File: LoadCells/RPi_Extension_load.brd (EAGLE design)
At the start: 80 x 50 mm, 42 parts, among them U1 AD7730BRUZ, U2 AD7730BRUZ, U3 AD7730BRUZ, U4 AD7730BRUZ, U5 AD7730BRUZ, U6 AD7730BRUZ, U7 AD7730BRUZ, U8 AD7730BRUZ, U9 STM32F103RCT6, Y1 ABM3B, Y2 KC2520B-C1

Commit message: retouched load cell board
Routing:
- net U1_AIN2_-: track 19.8 -> 24.6 mm
- net U2_AIN2_+: track 22.1 -> 20.5 mm
- net U2_AIN2_-: track 20.0 -> 21.5 mm
- net U2_AIN1_-: track 19.8 -> 18.4 mm
- net U2_AIN1_+: track 23.6 -> 22.4 mm
- net U5_AIN1_+: track 22.9 -> 22.0 mm
- net U1_AIN1_+: track 26.0 -> 25.3 mm
- net U8_AIN2_-: track 7.77 -> 8.43 mm
- net U8_AIN2_+: track 7.44 -> 8.05 mm
- net U6_AIN1_-: track 13.3 -> 13.9 mm

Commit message: added additional id jumpers to adc and dac board
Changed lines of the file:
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@@
 <wire x1="5.82" y1="16.28" x2="5.85" y2="16.28" width="0.4064" layer="16"/>
 <wire x1="5.85" y1="16.28" x2="5.85" y2="13.75" width="1.27" layer="16"/>
-<wire x1="5.82" y1="16.3" x2="5.82" y2="16.28" width="0.4064" layer="1"/>
 <wire x1="5.82" y1="13.65" x2="5.82" y2="13.74" width="0.4064" layer="16"/>
 </signal>

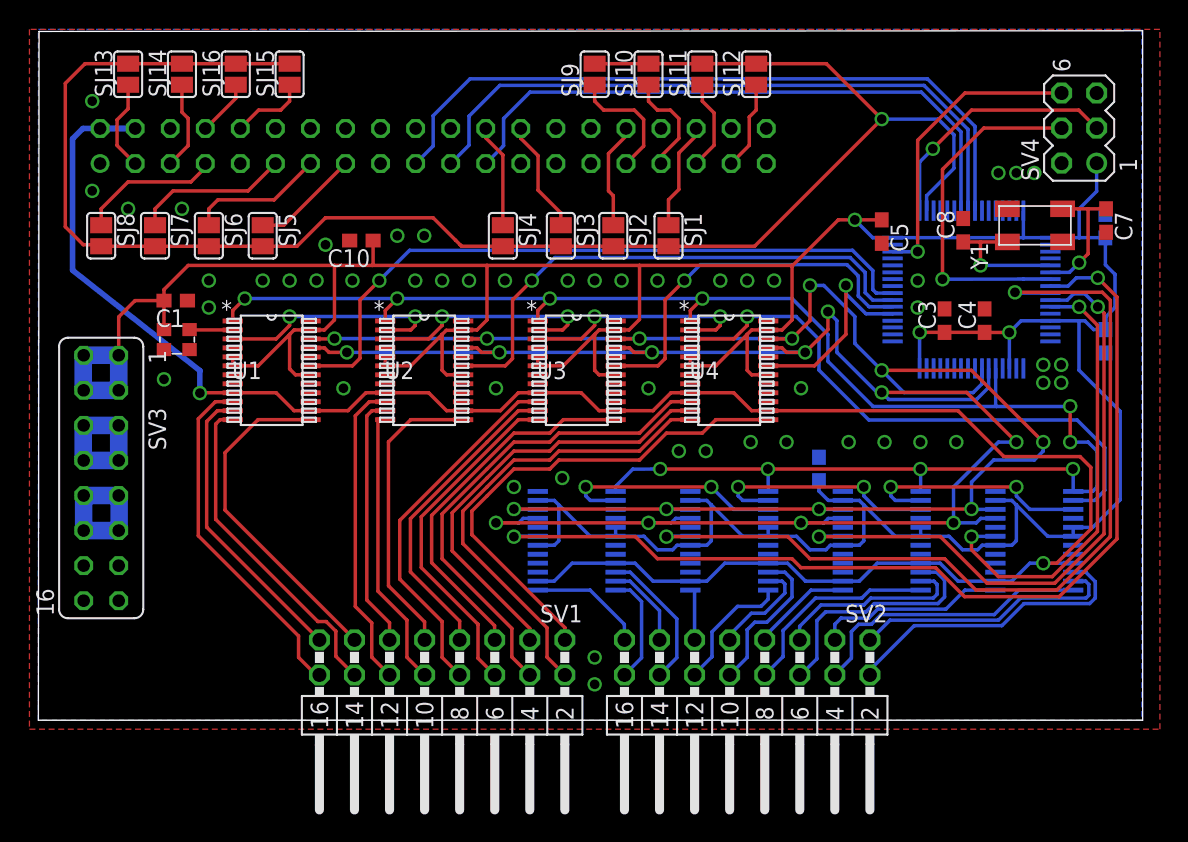
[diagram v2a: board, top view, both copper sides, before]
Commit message: cleaned up silklayer of load cell board
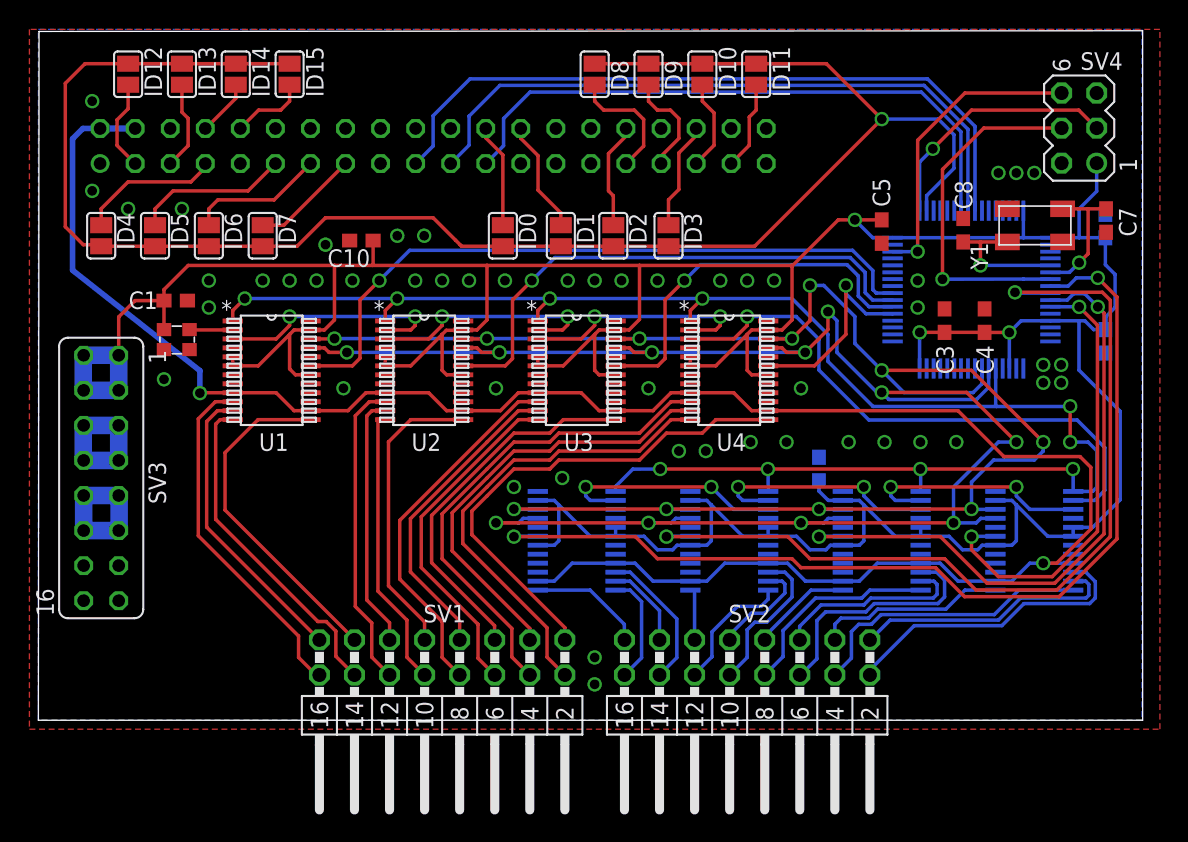
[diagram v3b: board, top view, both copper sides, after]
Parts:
- renumbered SJ1 to ID3, SJ10 to ID9, SJ11 to ID10, SJ12 to ID11, SJ13 to ID12, SJ14 to ID13, SJ15 to ID15, SJ16 to ID14, SJ2 to ID2, SJ3 to ID1, SJ4 to ID0, SJ5 to ID7, SJ6 to ID6, SJ7 to ID5, SJ8 to ID4, SJ9 to ID8
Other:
- board text added: "Hitzmann 2017"

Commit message: added more documentation
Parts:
- C1, C10, C9: value 0.1uf -> 100nF
- C2, C3, C4, C5, C6: value 100nf -> 100nF
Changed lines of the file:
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@@
 </element>
 <element name="Y2" library="kc2520b_c1" package="KC2520B-C1" value="KC2520B-C1" x="9.1" y="28.3" smashed="yes"/>
-<element name="C1" library="rcl" package="C0603" value="0.1uf" x="9.95" y="30.4" smashed="yes" rot="R180">
+<element name="C1" library="rcl" package="C0603" value="100nF" x="9.95" y="30.4" smashed="yes" rot="R180">
 <attribute name="NAME" x="8.635" y="31.065" size="1.27" layer="25" rot="R180"/>
 <attribute name="VALUE" x="10.585" y="32.305" size="1.27" layer="27" rot="R180"/>
 </element>
-<element name="C2" library="rcl" package="C0603" value="100nf" x="77.3" y="27.45" smashed="yes" rot="MR90">
+<element name="C2" library="rcl" package="C0603" value="100nF" x="77.3" y="27.45" smashed="yes" rot="MR90">
 <attribute name="NAME" x="78.335" y="26.215" size="1.27" layer="26" rot="MR90"/>
 <attribute name="VALUE" x="75.395" y="26.815" size="1.27" layer="28" rot="MR90"/>
 </element>
-<element name="C3" library="rcl" package="C0603" value="100nf" x="65.65" y="28.95" smashed="yes" rot="R90">
+<element name="C3" library="rcl" package="C0603" value="100nF" x="65.65" y="28.95" smashed="yes" rot="R90">
 <attribute name="NAME" x="66.315" y="25.065" size="1.27" layer="25" rot="R90"/>
 <attribute name="VALUE" x="67.555" y="28.315" size="1.27" layer="27" rot="R90"/>
 </element>
-<element name="C4" library="rcl" package="C0603" value="100nf" x="68.55" y="28.95" smashed="yes" rot="R90">
+<element name="C4" library="rcl" package="C0603" value="100nF" x="68.55" y="28.95" smashed="yes" rot="R90">
 <attribute name="NAME" x="69.215" y="25.065" size="1.27" layer="25" rot="R90"/>
 <attribute name="VALUE" x="70.455" y="28.315" size="1.27" layer="27" rot="R90"/>
 </element>
-<element name="C5" library="rcl" package="C0603" value="100nf" x="61.1" y="35.4" smashed="yes" rot="R270">
+<element name="C5" library="rcl" package="C0603" value="100nF" x="61.1" y="35.4" smashed="yes" rot="R270">
 <attribute name="NAME" x="60.435" y="39.285" size="1.27" layer="25" rot="R270"/>
 <attribute name="VALUE" x="59.195" y="36.035" size="1.27" layer="27" rot="R270"/>
 </element>
-<element name="C6" library="rcl" package="C0603" value="100nf" x="77.3" y="35.8" smashed="yes" rot="MR90">
+<element name="C6" library="rcl" package="C0603" value="100nF" x="77.3" y="35.8" smashed="yes" rot="MR90">
 <attribute name="NAME" x="78.335" y="34.565" size="1.27" layer="26" rot="MR90"/>
 <attribute name="VALUE" x="75.395" y="35.165" size="1.27" layer="28" rot="MR90"/>
@@
 <attribute name="VALUE" x="68.905" y="34.865" size="1.27" layer="27" rot="R90"/>
 </element>
-<element name="C9" library="rcl" package="C0603" value="0.1uf" x="56.55" y="18.2" smashed="yes" rot="MR90">
+<element name="C9" library="rcl" package="C0603" value="100nF" x="56.55" y="18.2" smashed="yes" rot="MR90">
 <attribute name="NAME" x="55.935" y="19.715" size="1.27" layer="26" rot="MR90"/>
 <attribute name="VALUE" x="54.645" y="17.565" size="1.27" layer="28" rot="MR90"/>
 </element>
-<element name="C10" library="rcl" package="C0603" value="0.1uf" x="23.4" y="34.75" rot="R180"/>
+<element name="C10" library="rcl" package="C0603" value="100nF" x="23.4" y="34.75" rot="R180"/>
 <element name="ID8" library="jumper" package="SJ" value="" x="40.3" y="46.8" smashed="yes" rot="R90">
 <attribute name="NAME" x="42.757" y="45.149" size="1.27" layer="25" ratio="10" rot="R90"/>
